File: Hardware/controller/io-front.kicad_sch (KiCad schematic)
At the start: 24 parts

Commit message: hw: add charger for RTC
- added RTC supercapacitor

- added the charging circuit for the RTC (with adjustment for voltage
  and all that fun stuff) based around a bonus linear regulator for the
  supercap

- minor tweaks all around: add more JLCPCB part numbers and fixed some
  footprints for some components
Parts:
- U: JLCPCB (none) -> C25804
- U: JLCPCB (none) -> C4190
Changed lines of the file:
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@@
+      (effects (font (size 1.27 1.27)) hide)
+    )
+    (property "JLCPCB" "C25804" (id 5) (at 37.465 189.865 90)
       (effects (font (size 1.27 1.27)) hide)
     )
@@
       (effects (font (size 1.27 1.27)) hide)
     )
+    (property "JLCPCB" "C25804" (id 5) (at 37.465 165.1 90)
+      (effects (font (size 1.27 1.27)) hide)
+    )
     (pin "1")
     (pin "2")
@@
       (effects (font (size 1.27 1.27)) hide)
     )
+    (property "JLCPCB" "C4190" (id 5) (at 37.465 181.61 90)
+      (effects (font (size 1.27 1.27)) hide)
+    )
     (pin "1")
     (pin "2")
@@
       (effects (font (size 1.27 1.27)) hide)
     )
+    (property "JLCPCB" "C4190" (id 5) (at 37.465 173.355 90)
+      (effects (font (size 1.27 1.27)) hide)
+    )

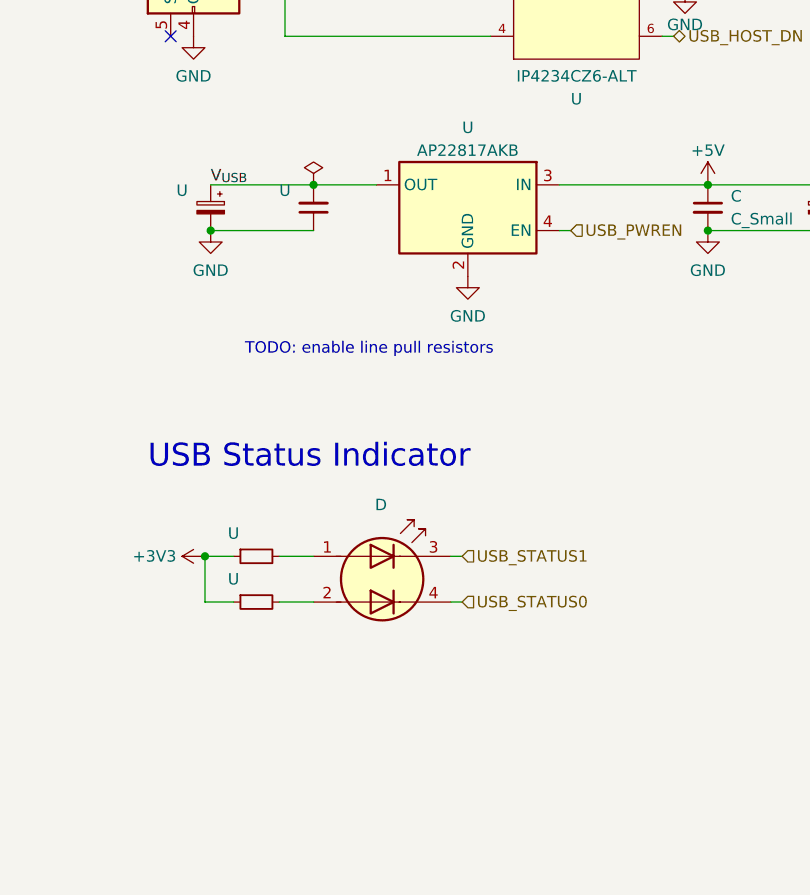
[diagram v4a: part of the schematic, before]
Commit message: hw: add more part numbers, cleanup
- Added JLCPCB part numbers for more passive components

- Added a status LED for the rear of the board (next to the device USB
  port)
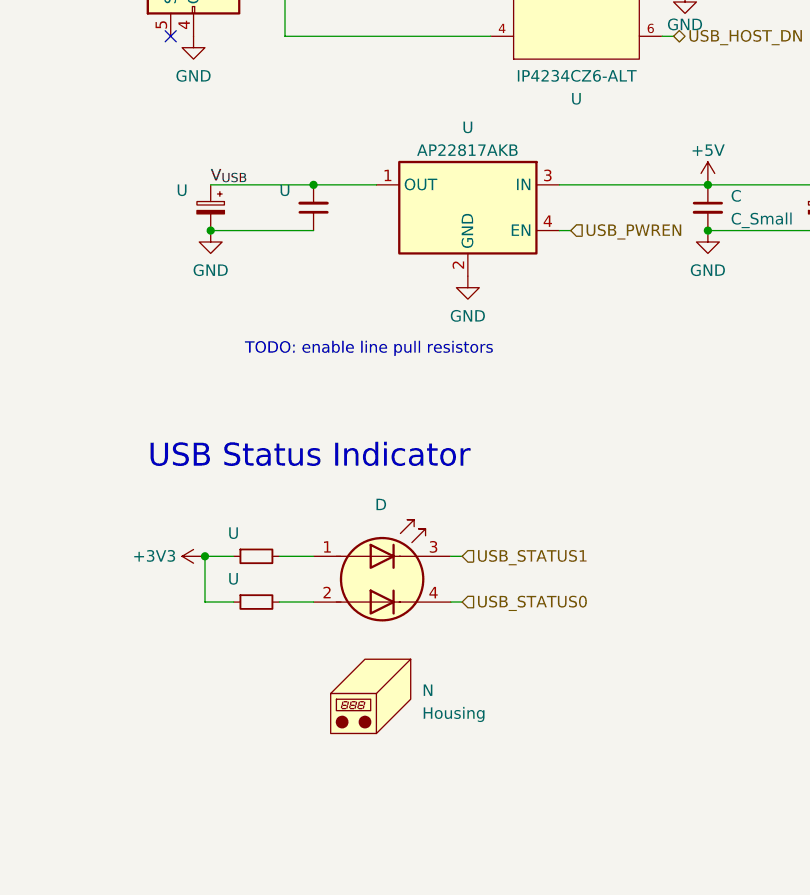
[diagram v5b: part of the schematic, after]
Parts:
- added N: Housing, symbol Mechanical:Housing
- C: JLCPCB (none) -> C15849
- U: JLCPCB (none) -> C21190
- U: JLCPCB (none) -> C7171
- U: JLCPCB (none) -> C23138
- U: JLCPCB (none) -> C14663
- U: JLCPCB (none) -> C20526
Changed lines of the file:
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@@
+      (effects (font (size 1.27 1.27)) hide)
+    )
+    (property "JLCPCB" "C21190" (id 5) (at 139.065 109.855 90)
       (effects (font (size 1.27 1.27)) hide)
     )
@@
     )
     (property "MPN" "TAJA106K016RNJ" (id 4) (at 36.83 31.115 0)
+      (effects (font (size 1.27 1.27)) hide)
+    )
+    (property "JLCPCB" "C7171" (id 5) (at 36.83 31.115 0)
       (effects (font (size 1.27 1.27)) hide)
     )
@@
     (pin "2")
   )
+  (symbol (lib_id "Mechanical:Housing") (at 153.035 120.015 0) (unit 1)
+    (in_bom yes) (on_board yes) (fields_autoplaced)
+    (default_instance (reference "N") (unit 1) (value "Housing") (footprint ""))
+    (property "Reference" "N" (id 0) (at 157.48 119.6975 0)
+      (effects (font (size 1.27 1.27)) (justify left))
+    )
+    (property "Value" "Housing" (id 1) (at 157.48 122.2375 0)
+      (effects (font (size 1.27 1.27)) (justify left))
+    )
+    (property "Footprint" "" (id 2) (at 154.305 118.745 0)
+      (effects (font (size 1.27 1.27)) hide)
+    )
+    (property "Datasheet" "~" (id 3) (at 154.305 118.745 0)
+      (effects (font (size 1.27 1.27)) hide)
+    )
+  )
   (symbol (lib_id "power:GND") (at 189.23 68.58 0) (unit 1)
     (in_bom yes) (on_board yes)
@@
     )
     (property "Datasheet" "" (id 3) (at 31.75 150.495 0)
-      (effects (font (size 1.27 1.27)) hide)
-    )
-    (pin "1")
-  )
-  (symbol (lib_id "power:PWR_FLAG") (at 145.415 63.5 0) (unit 1)
-    (in_bom yes) (on_board yes) (fields_autoplaced)
-    (default_instance (reference "#FLG") (unit 1) (value "PWR_FLAG") (footprint ""))
-    (property "Reference" "#FLG" (id 0) (at 145.415 61.595 0)
-      (effects (font (size 1.27 1.27)) hide)
-    )
-    (property "Value" "PWR_FLAG" (id 1) (at 145.415 59.69 0)
-      (effects (font (size 1.27 1.27)) hide)
-    )
-    (property "Footprint" "" (id 2) (at 145.415 63.5 0)
-      (effects (font (size 1.27 1.27)) hide)
-    )
-    (property "Datasheet" "~" (id 3) (at 145.415 63.5 0)
       (effects (font (size 1.27 1.27)) hide)
     )
@@
       (effects (font (size 1.27 1.27)) hide)
     )
+    (property "JLCPCB" "C15849" (id 4) (at 189.23 66.04 0)
+      (effects (font (size 1.27 1.27)) hide)
+    )
     (pin "1")
     (pin "2")
@@
     )
     (property "MPN" "" (id 4) (at 108.585 163.83 0)
+      (effects (font (size 1.27 1.27)) hide)
+    )
+    (property "JLCPCB" "C23138" (id 5) (at 108.585 163.83 0)
       (effects (font (size 1.27 1.27)) hide)
     )
@@
       (effects (font (size 1.27 1.27)) hide)
     )
+    (property "JLCPCB" "C21190" (id 5) (at 139.065 104.775 90)
+      (effects (font (size 1.27 1.27)) hide)
+    )
     (pin "1")
     (pin "2")
@@
       (effects (font (size 1.27 1.27)) hide)
     )
+    (property "JLCPCB" "C14663" (id 5) (at 145.415 66.04 0)
+      (effects (font (size 1.27 1.27)) hide)
+    )
     (pin "1")
     (pin "2")
@@
       (effects (font (size 1.27 1.27)) hide)
     )
+    (property "JLCPCB" "C7171" (id 5) (at 201.93 66.04 0)
+      (effects (font (size 1.27 1.27)) hide)
+    )
     (pin "1")
     (pin "2")
@@
       (effects (font (size 1.27 1.27)) hide)
     )
+    (property "JLCPCB" "C20526" (id 5) (at 111.125 180.975 0)
+      (effects (font (size 1.27 1.27)) hide)
+    )
     (pin "1")
     (pin "2")
@@
       (effects (font (size 1.27 1.27)) hide)
     )
+    (property "JLCPCB" "C14663" (id 5) (at 26.035 31.115 0)
+      (effects (font (size 1.27 1.27)) hide)
+    )
     (pin "1")
     (pin "2")
@@
       (effects (font (size 1.27 1.27)) hide)
     )
-    (property "MPn" "" (id 4) (at 121.285 180.975 0)
-      (effects (font (size 1.27 1.27)) hide)
-    )
+    (property "MPN" "" (id 4) (at 121.285 180.975 0)
+      (effects (font (size 1.27 1.27)) hide)
+    )
+    (property "JLCPCB" "C23138" (id 5) (at 121.285 180.975 90)
+      (effects (font (size 1.27 1.27)) hide)
+    )

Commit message: hw: fix part numbers
- fixed missing or incorrect MPN and JLCPCB part numbers for various
  components; most should have either one of these now
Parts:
- C: MPN (none) -> CL10B105KP8NFNC
- J: JLCPCB (none) -> C231436
- N: MPN (none) -> SLP3-150-300-F
- U: MPN (none) -> IP4234CZ6,125
- U: JLCPCB (none) -> C1015
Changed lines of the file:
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@@
+      (effects (font (size 1.27 1.27)) hide)
+    )
+    (property "JLCPCB" "C231436" (id 4) (at 69.215 60.96 0)
       (effects (font (size 1.27 1.27)) hide)
     )
@@
       (effects (font (size 1.27 1.27)) hide)
     )
+    (property "MPN" "SLP3-150-300-F" (id 5) (at 153.035 120.015 0)
+      (effects (font (size 1.27 1.27)) hide)
+    )
   )
   (symbol (lib_id "power:GND") (at 189.23 68.58 0) (unit 1)
@@
     (property "Datasheet" "https://assets.nexperia.com/documents/data-sheet/IP4234CZ6.pdf" (id 3) (at 167.64 74.93 0)
       (effects (font (size 1.27 1.27)) (justify left) hide)
+    )
+    (property "MPN" "IP4234CZ6,125" (id 4) (at 167.64 49.53 0)
+      (effects (font (size 1.27 1.27)) hide)
     )
     (pin "1")
@@
       (effects (font (size 1.27 1.27)) hide)
     )
+    (property "MPN" "CL10B105KP8NFNC" (id 5) (at 189.23 66.04 0)
+      (effects (font (size 1.27 1.27)) hide)
+    )
     (pin "1")
     (pin "2")
@@
       (effects (font (size 1.27 1.27)) hide)
     )
+    (property "JLCPCB" "C1015" (id 5) (at 51.435 28.575 90)
+      (effects (font (size 1.27 1.27)) hide)
+    )

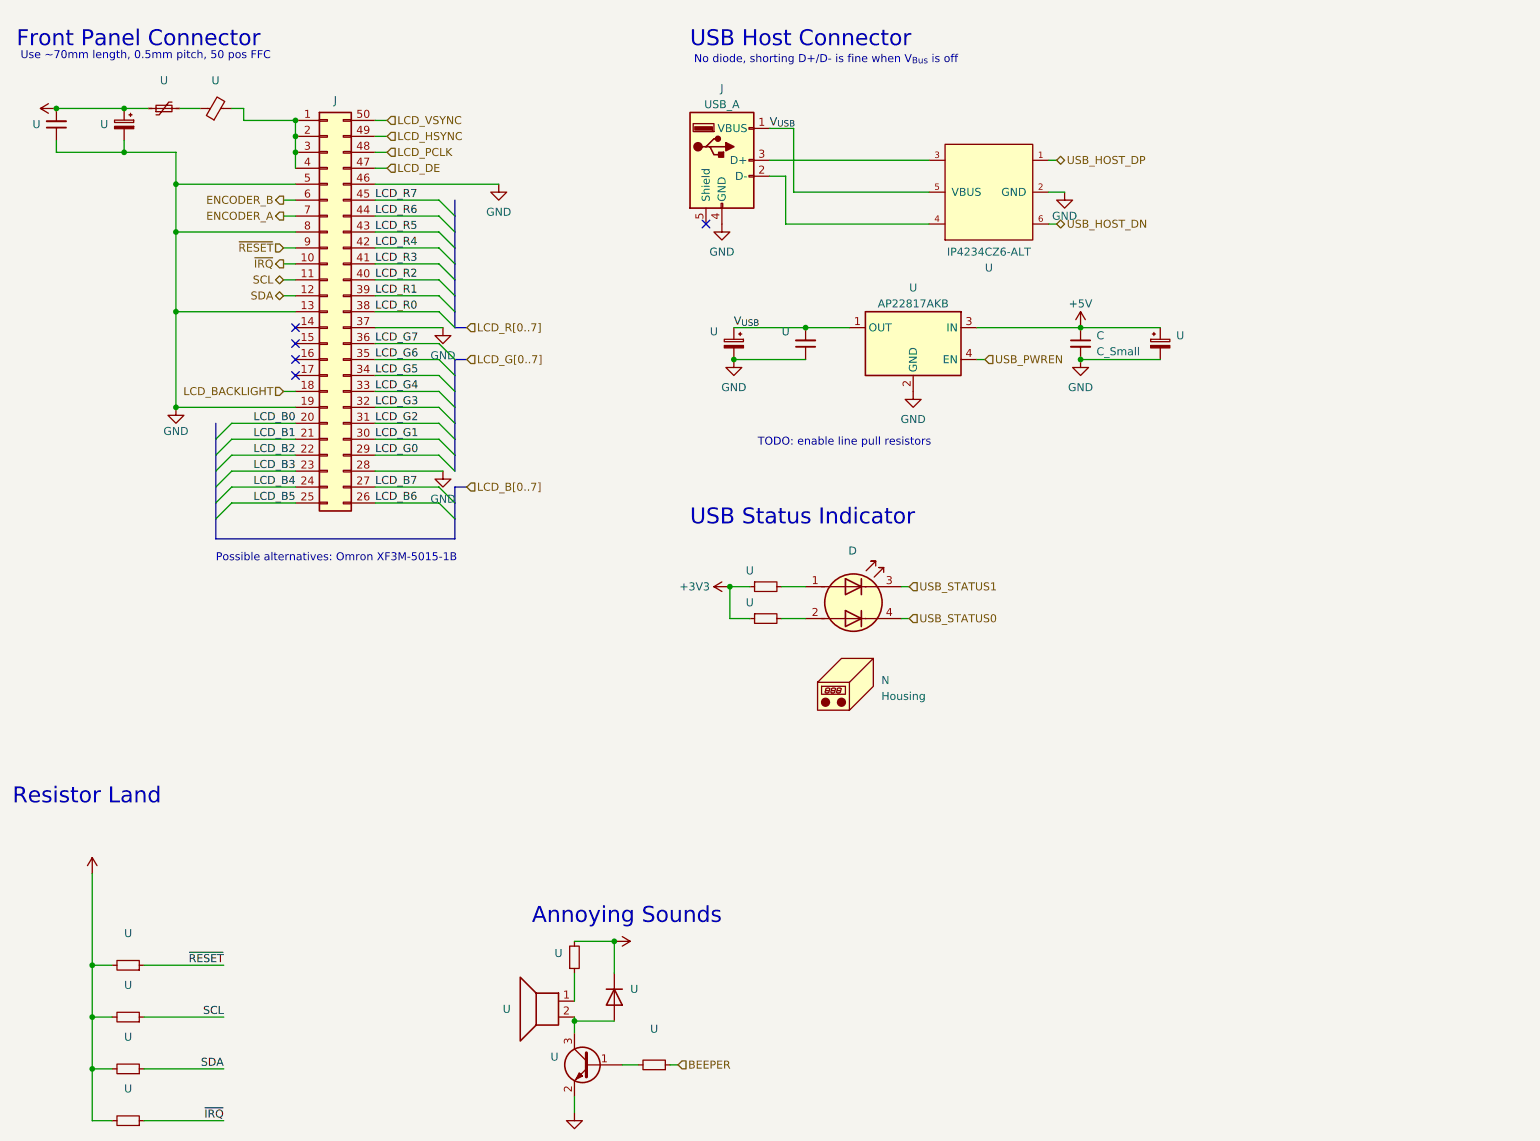
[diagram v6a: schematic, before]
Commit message: hw: add aux analog out
- Added an auxiliary analog output port (driven from the STM32MP1
  on-board DAC, through a buffer, which scales it up to 0-4V range) to
  be connected to a front panel BNC

  It probably needs some sort of ESD protection
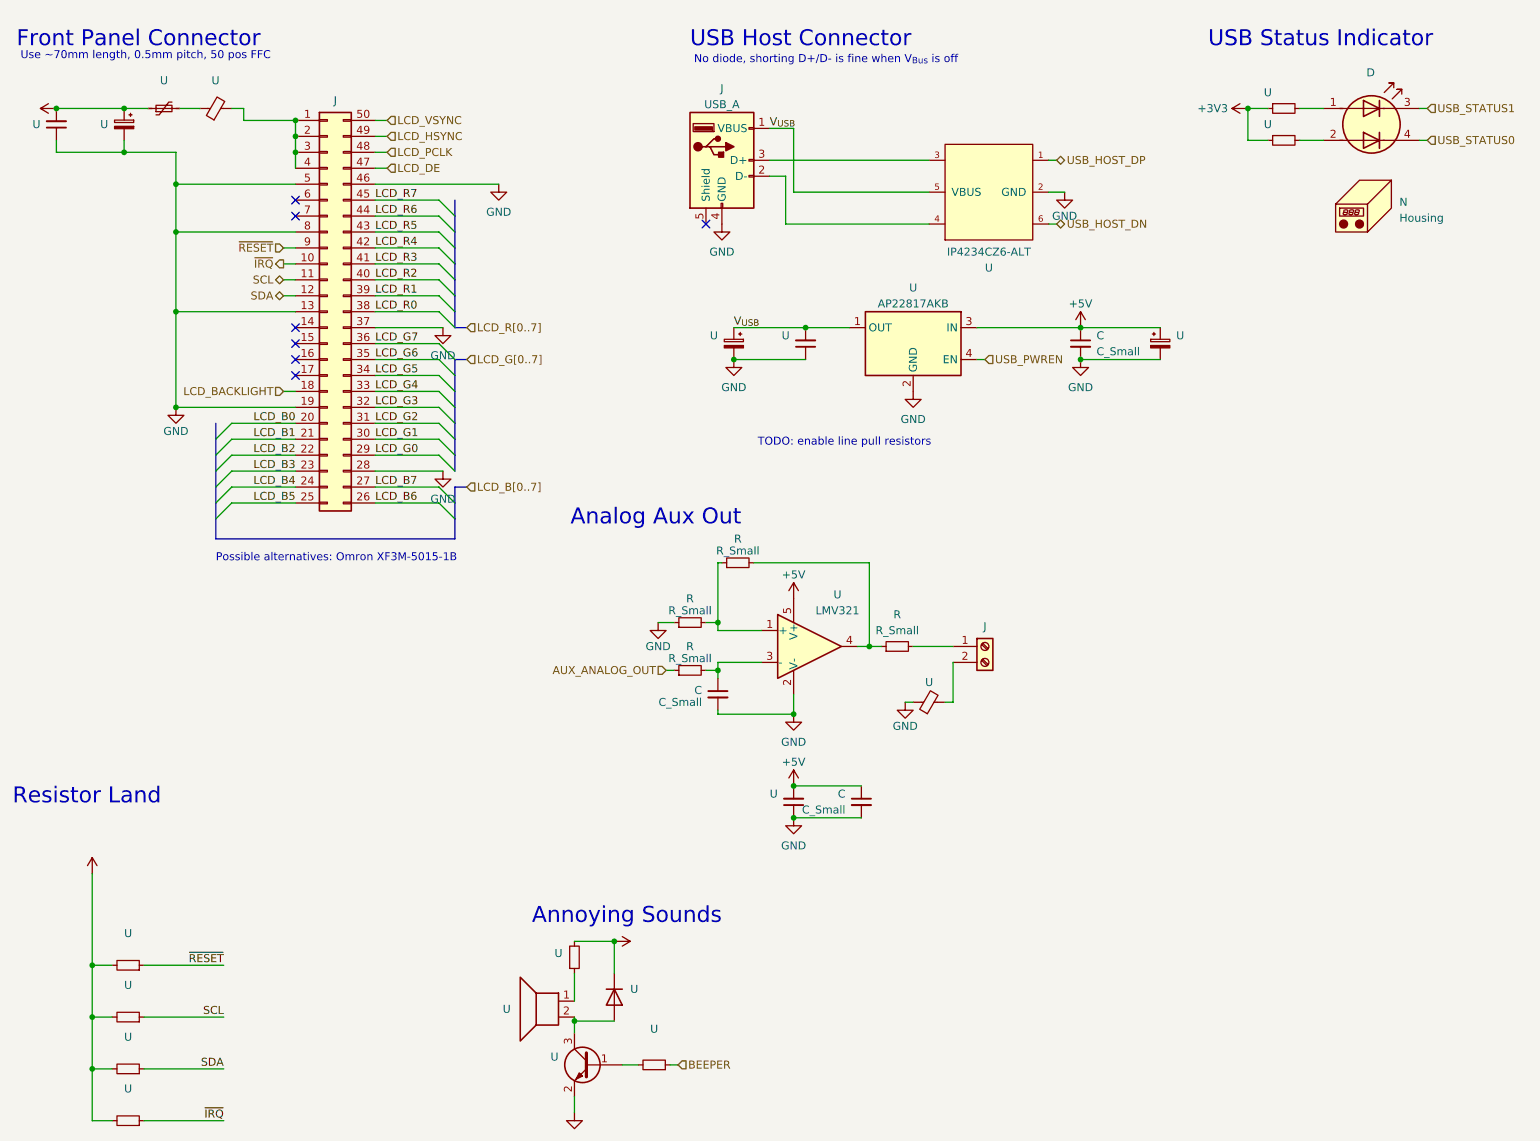
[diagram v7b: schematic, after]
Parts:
- added C (x2): C_Small, symbol Device:C_Small
- added J: Screw_Terminal_01x02, symbol Connector:Screw_Terminal_01x02
- added R (x4): R_Small, symbol Device:R_Small
- added U: (no value), symbol Device:FerriteBead_Small
- added U: (no value), symbol Device:C_Small
- added U: LMV321, symbol Amplifier_Operational:LMV321
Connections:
- net +5V: now also C.1, U.2, U.5 (V+)
- net GND: now also C.2, C.2, R.1, U.1, U.1, U.2 (V-)
- net ENCODER_A: no longer names the net of J.7 (Pin_7)
- net ENCODER_B: no longer names the net of J.6 (Pin_6)
- new net: C.1, R.2, U.3 (-)
- new net: J.2 (Pin_2), U.2
- new net: R.1, R.2, U.4
- new net: J.1 (Pin_1), R.2
- new net: R.1, R.2, U.1 (+)
- new net AUX_ANALOG_OUT: R.1
- no-connect marks 5 -> 7
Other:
- note added: "Analog Aux Out"
- moved on the sheet: D, N, U
